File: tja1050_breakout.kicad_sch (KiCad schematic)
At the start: 10 parts, among them J1 Termination Jumper, J2 CAN Jumper, J3 Phoenix Block, J4 Jumper, J5 CANS Jumper, U1 TJA1051T

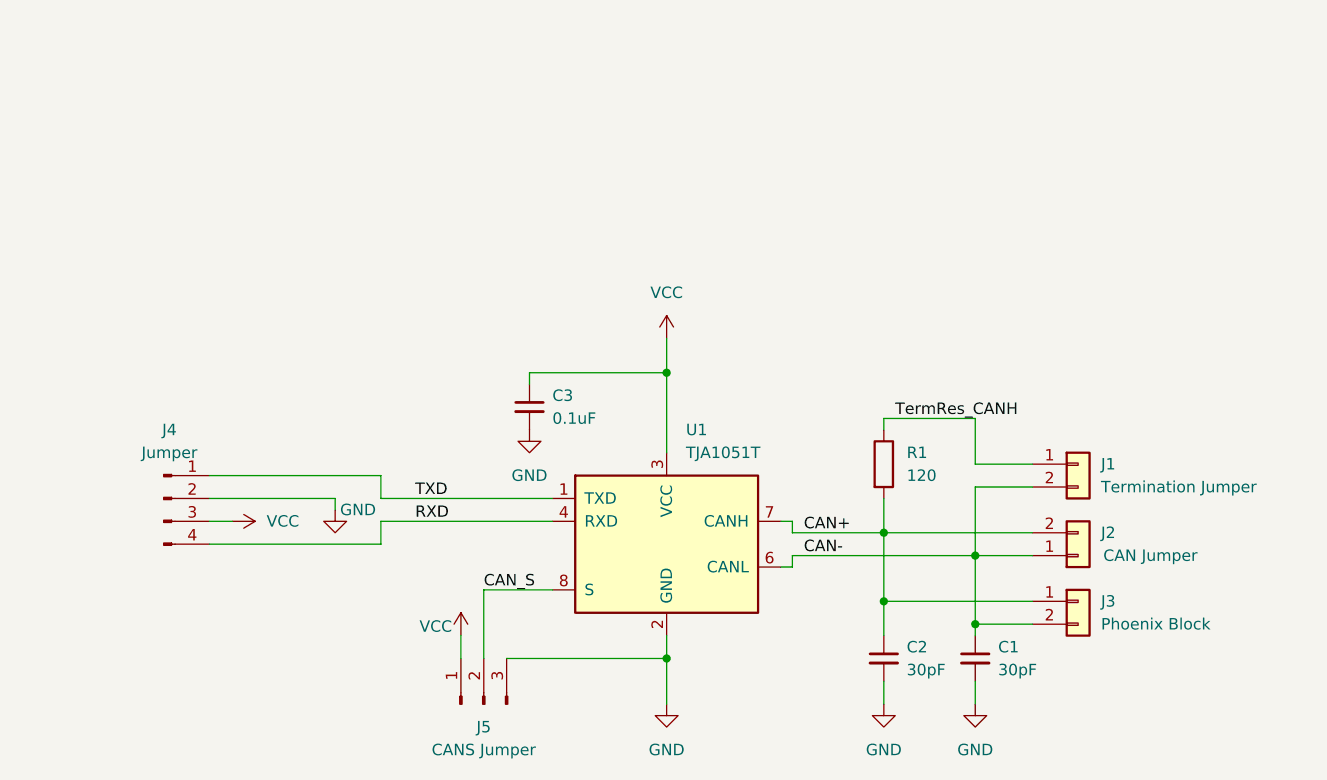
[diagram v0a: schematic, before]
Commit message: update schematic
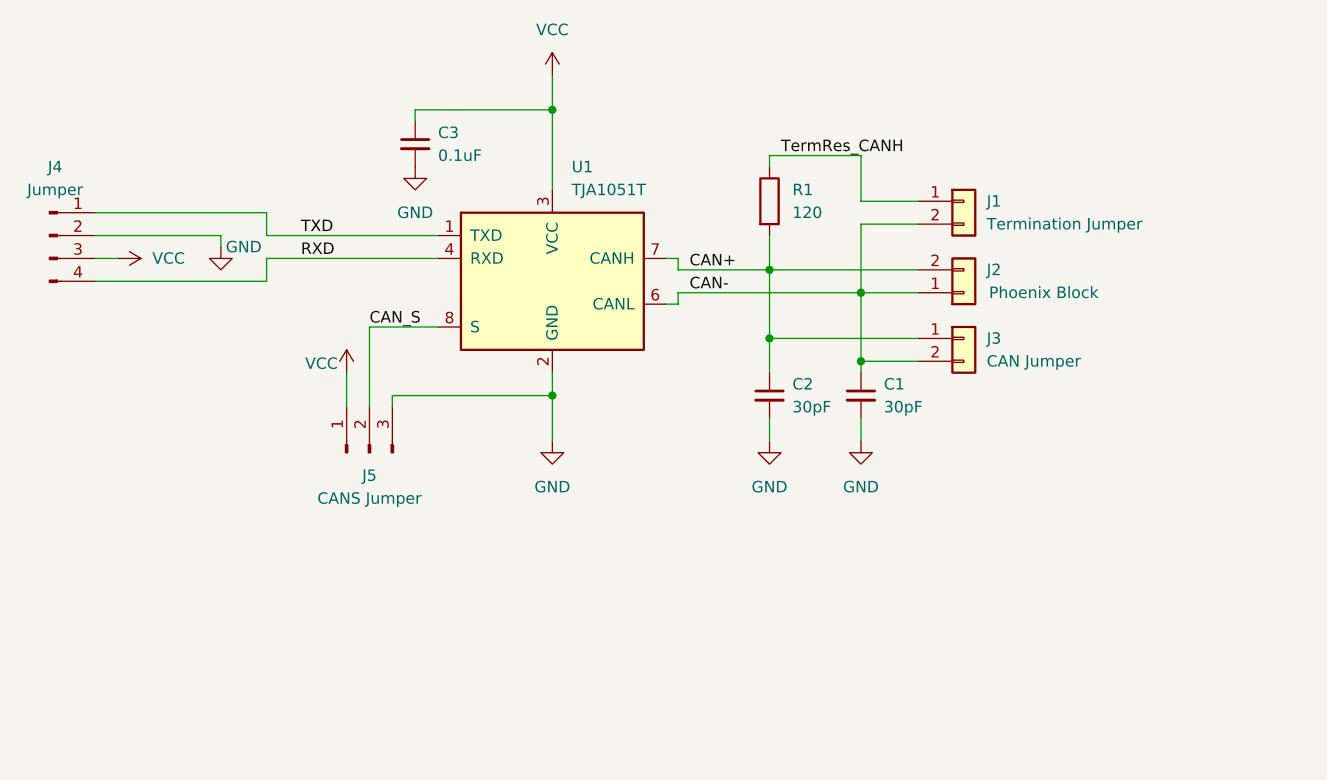
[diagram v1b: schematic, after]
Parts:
- J2: value CAN Jumper -> Phoenix Block
- J3: value Phoenix Block -> CAN Jumper
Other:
- title: (none) -> TJA1051 Breakout Board
- moved on the sheet: C1, C2, C3, J1, J2, J3, J4, J5, R1, U1

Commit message: update  bom
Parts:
- J1, J3: MPN (none) -> C32713268
- J4: MPN (none) -> C32713270
- J5: MPN (none) -> C5360899
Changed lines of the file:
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@@
+			)
+		)
+		(property "MPN" "C32713268"
+			(at 146.05 48.26 0)
+			(effects
+				(font
+					(size 1.27 1.27)
+				)
+				(hide yes)
 			)
 		)
@@
 			)
 		)
+		(property "MPN" "C5360899"
+			(at 80.01 76.2 90)
+			(effects
+				(font
+					(size 1.27 1.27)
+				)
+				(hide yes)
+			)
+		)
 		(pin "1"
 		)
@@
 			)
 		)
+		(property "MPN" "C32713270"
+			(at 44.45 52.07 0)
+			(effects
+				(font
+					(size 1.27 1.27)
+				)
+				(hide yes)
+			)
+		)
 		(pin "3"
 		)
@@
 			(at 146.05 63.5 0)
 			(effects
+				(font
+					(size 1.27 1.27)
+				)
+				(hide yes)
+			)
+		)
+		(property "MPN" "C32713268"
+			(at 146.05 63.5 0)
+			(effects

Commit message: v1.1 initial
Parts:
- C1, C2: footprint Capacitor_SMD:C_0402_1005Metric -> Capacitor_SMD:C_0603_1608Metric; MPN C466228 -> C1658
- C3: footprint Capacitor_SMD:C_0402_1005Metric -> Capacitor_SMD:C_0603_1608Metric; MPN C1525 -> C14663
- R1: footprint Resistor_SMD:R_0402_1005Metric -> Resistor_SMD:R_0603_1608Metric; MPN C25079 -> C22787
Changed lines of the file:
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@@
 			)
 		)
-		(property "Footprint" "Capacitor_SMD:C_0402_1005Metric"
+		(property "Footprint" "Capacitor_SMD:C_0603_1608Metric"
 			(at 124.46 69.85 0)
 			(effects
@@
 			)
 		)
-		(property "MPN" "C466228"
+		(property "MPN" "C1658"
 			(at 124.46 69.85 0)
 			(effects
@@
 			)
 		)
-		(property "Footprint" "Capacitor_SMD:C_0402_1005Metric"
+		(property "Footprint" "Capacitor_SMD:C_0603_1608Metric"
 			(at 85.09 41.91 0)
 			(effects
@@
 			)
 		)
-		(property "MPN" "C1525"
+		(property "MPN" "C14663"
 			(at 85.09 41.91 0)
 			(effects
@@
 			)
 		)
-		(property "Footprint" "Resistor_SMD:R_0402_1005Metric"
+		(property "Footprint" "Resistor_SMD:R_0603_1608Metric"
 			(at 122.682 48.26 90)
 			(effects
@@
 			)
 		)
-		(property "MPN" "C25079"
+		(property "MPN" "C22787"
 			(at 124.46 48.26 0)
 			(effects
@@
 			)
 		)
-		(property "Footprint" "Capacitor_SMD:C_0402_1005Metric"
+		(property "Footprint" "Capacitor_SMD:C_0603_1608Metric"
 			(at 134.62 69.85 0)
 			(effects
@@
 			)
 		)
-		(property "MPN" "C466228"
+		(property "MPN" "C1658"
 			(at 134.62 69.85 0)
 			(effects

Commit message: update mpn
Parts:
- C1, C2: LCSC (none) -> C1658; MPN C1658 -> (none)
- C3: LCSC (none) -> C14663; MPN C14663 -> (none)
- J1, J3: LCSC (none) -> C32713268; MPN C32713268 -> (none)
- J2: LCSC (none) -> C474950; MPN C474950 -> (none)
- J4: LCSC (none) -> C32713270; MPN C32713270 -> (none)
- J5: LCSC (none) -> C5360899; MPN C5360899 -> (none)
- R1: LCSC (none) -> C22787; MPN C22787 -> (none)
- U1: LCSC (none) -> C18387; MPN C18387 -> (none)
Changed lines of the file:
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@@
 			)
 		)
-		(property "MPN" "C1658"
+		(property "LCSC" "C1658"
 			(at 124.46 69.85 0)
 			(effects
@@
 			)
 		)
-		(property "MPN" "C32713268"
+		(property "LCSC" "C32713268"
 			(at 146.05 48.26 0)
 			(effects
@@
 			)
 		)
-		(property "MPN" "C474950"
+		(property "LCSC" "C474950"
 			(at 146.05 58.42 0)
 			(effects
@@
 			)
 		)
-		(property "MPN" "C18387"
+		(property "LCSC" "C18387"
 			(at 100.33 57.15 0)
 			(effects
@@
 			)
 		)
-		(property "MPN" "C5360899"
+		(property "LCSC" "C5360899"
 			(at 80.01 76.2 90)
 			(effects
@@
 			)
 		)
-		(property "MPN" "C14663"
+		(property "LCSC" "C14663"
 			(at 85.09 41.91 0)
 			(effects
@@
 			)
 		)
-		(property "MPN" "C22787"
+		(property "LCSC" "C22787"
 			(at 124.46 48.26 0)
 			(effects
@@
 			)
 		)
-		(property "MPN" "C1658"
+		(property "LCSC" "C1658"
 			(at 134.62 69.85 0)
 			(effects
@@
 			)
 		)
-		(property "MPN" "C32713270"
+		(property "LCSC" "C32713270"
 			(at 44.45 52.07 0)
 			(effects
@@
 			)
 		)
-		(property "MPN" "C32713268"
+		(property "LCSC" "C32713268"
 			(at 146.05 63.5 0)
 			(effects
